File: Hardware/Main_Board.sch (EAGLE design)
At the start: 14 parts

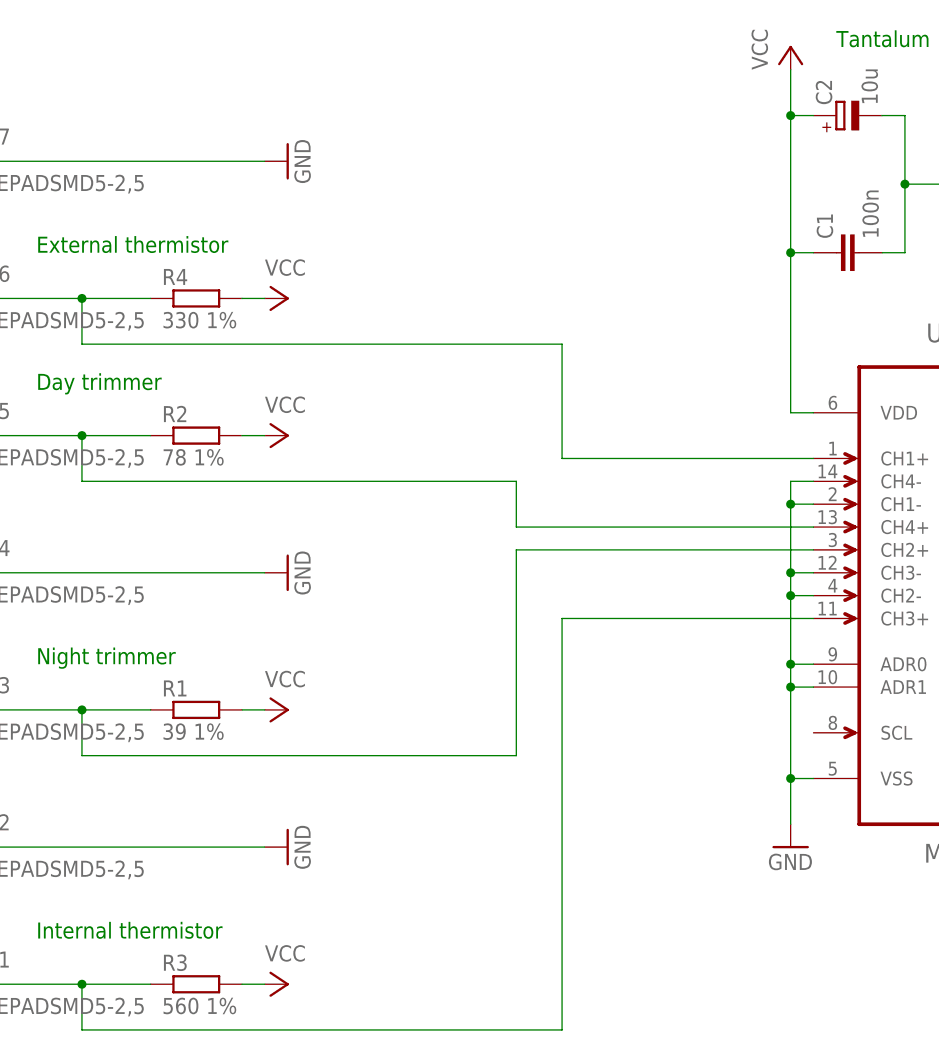
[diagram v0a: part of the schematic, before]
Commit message: Used more generic resistors in the voltage dividers.
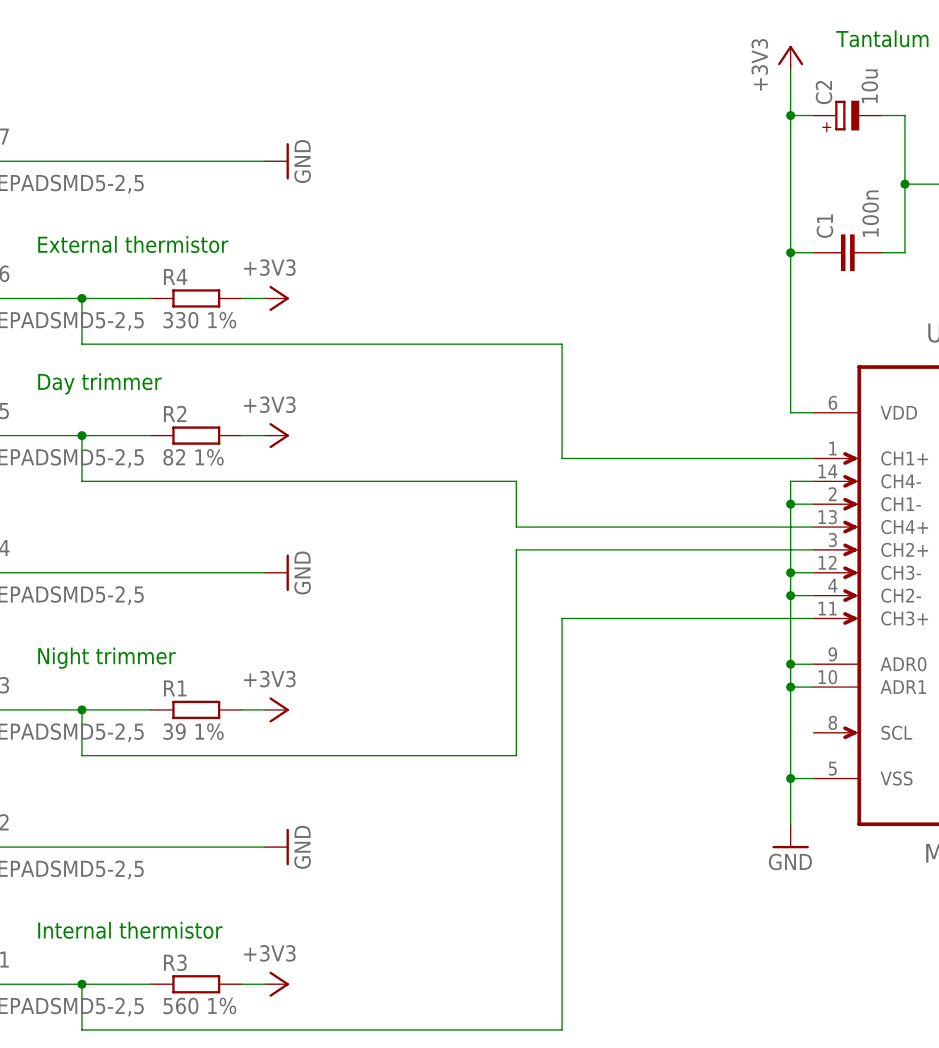
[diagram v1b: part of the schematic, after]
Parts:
- R2: value 78 1% -> 82 1%
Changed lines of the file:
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@@
 <part name="R1" library="resistor" deviceset="R-EU_" device="0207/10" value="39 1%"/>
 <part name="PAD3" library="wirepad" deviceset="WIREPAD" device="SMD5-2,5"/>
-<part name="P+1" library="supply1" deviceset="VCC" device=""/>
+<part name="P+1" library="supply1" deviceset="+3V3" device=""/>
 <part name="U$1" library="MCP3428" deviceset="MCP3428-E/SL" device=""/>
 <part name="PAD5" library="wirepad" deviceset="WIREPAD" device="SMD5-2,5"/>
-<part name="R2" library="resistor" deviceset="R-EU_" device="0207/10" value="78 1%"/>
-<part name="P+2" library="supply1" deviceset="VCC" device=""/>
+<part name="R2" library="resistor" deviceset="R-EU_" device="0207/10" value="82 1%"/>
+<part name="P+2" library="supply1" deviceset="+3V3" device=""/>
 <part name="PAD4" library="wirepad" deviceset="WIREPAD" device="SMD5-2,5"/>
 <part name="GND2" library="supply1" deviceset="GND" device=""/>
@@
 <part name="GND3" library="supply1" deviceset="GND" device=""/>
 <part name="R3" library="resistor" deviceset="R-EU_" device="0207/10" value="560 1%"/>
-<part name="P+3" library="supply1" deviceset="VCC" device=""/>
+<part name="P+3" library="supply1" deviceset="+3V3" device=""/>
 <part name="GND4" library="supply1" deviceset="GND" device=""/>
-<part name="P+4" library="supply1" deviceset="VCC" device=""/>
+<part name="P+4" library="supply1" deviceset="+3V3" device=""/>
 <part name="R4" library="resistor" deviceset="R-EU_" device="0207/10" value="330 1%"/>
-<part name="P+5" library="supply1" deviceset="VCC" device=""/>
+<part name="P+5" library="supply1" deviceset="+3V3" device=""/>
 <part name="PAD6" library="wirepad" deviceset="WIREPAD" device="SMD5-2,5"/>
 <part name="PAD7" library="wirepad" deviceset="WIREPAD" device="SMD5-2,5"/>
@@
 <instance part="R1" gate="G$1" x="-17.78" y="124.46"/>
 <instance part="PAD3" gate="G$1" x="-43.18" y="124.46"/>
-<instance part="P+1" gate="VCC" x="-7.62" y="124.46" rot="R270"/>
+<instance part="P+1" gate="G$1" x="-7.62" y="124.46" rot="R270"/>
 <instance part="U$1" gate="A" x="68.58" y="139.7"/>
 <instance part="PAD5" gate="G$1" x="-43.18" y="154.94"/>
 <instance part="R2" gate="G$1" x="-17.78" y="154.94"/>
-<instance part="P+2" gate="VCC" x="-7.62" y="154.94" rot="R270"/>
+<instance part="P+2" gate="G$1" x="-7.62" y="154.94" rot="R270"/>
 <instance part="PAD4" gate="G$1" x="-43.18" y="139.7"/>
 <instance part="GND2" gate="1" x="-7.62" y="139.7" rot="R90"/>
@@
 <instance part="GND3" gate="1" x="-7.62" y="109.22" rot="R90"/>
 <instance part="R3" gate="G$1" x="-17.78" y="93.98"/>
-<instance part="P+3" gate="VCC" x="-7.62" y="93.98" rot="R270"/>
+<instance part="P+3" gate="G$1" x="-7.62" y="93.98" rot="R270"/>
 <instance part="GND4" gate="1" x="48.26" y="109.22"/>
-<instance part="P+4" gate="VCC" x="48.26" y="198.12"/>
+<instance part="P+4" gate="G$1" x="48.26" y="198.12"/>
 <instance part="R4" gate="G$1" x="-17.78" y="170.18"/>
-<instance part="P+5" gate="VCC" x="-7.62" y="170.18" rot="R270"/>
+<instance part="P+5" gate="G$1" x="-7.62" y="170.18" rot="R270"/>
 <instance part="PAD6" gate="G$1" x="-43.18" y="170.18"/>
 <instance part="PAD7" gate="G$1" x="-43.18" y="185.42"/>
@@
 <net name="VCC" class="0">
 <segment>
-<pinref part="P+1" gate="VCC" pin="VCC"/>
+<pinref part="P+1" gate="G$1" pin="+3V3"/>
 <pinref part="R1" gate="G$1" pin="2"/>
 <wire x1="-10.16" y1="124.46" x2="-12.7" y2="124.46" width="0.1524" layer="91"/>
 </segment>
 <segment>
-<pinref part="P+2" gate="VCC" pin="VCC"/>
+<pinref part="P+2" gate="G$1" pin="+3V3"/>
 <pinref part="R2" gate="G$1" pin="2"/>
 <wire x1="-10.16" y1="154.94" x2="-12.7" y2="154.94" width="0.1524" layer="91"/>
 </segment>
 <segment>
-<pinref part="P+3" gate="VCC" pin="VCC"/>
+<pinref part="P+3" gate="G$1" pin="+3V3"/>
 <pinref part="R3" gate="G$1" pin="2"/>
 <wire x1="-10.16" y1="93.98" x2="-12.7" y2="93.98" width="0.1524" layer="91"/>
 </segment>
 <segment>
-<pinref part="P+4" gate="VCC" pin="VCC"/>
+<pinref part="P+4" gate="G$1" pin="+3V3"/>
 <wire x1="48.26" y1="195.58" x2="48.26" y2="190.5" width="0.1524" layer="91"/>
 <pinref part="U$1" gate="A" pin="VDD"/>
@@
 <segment>
 <pinref part="R4" gate="G$1" pin="2"/>
-<pinref part="P+5" gate="VCC" pin="VCC"/>
+<pinref part="P+5" gate="G$1" pin="+3V3"/>
 <wire x1="-12.7" y1="170.18" x2="-10.16" y2="170.18" width="0.1524" layer="91"/>
 </segment>

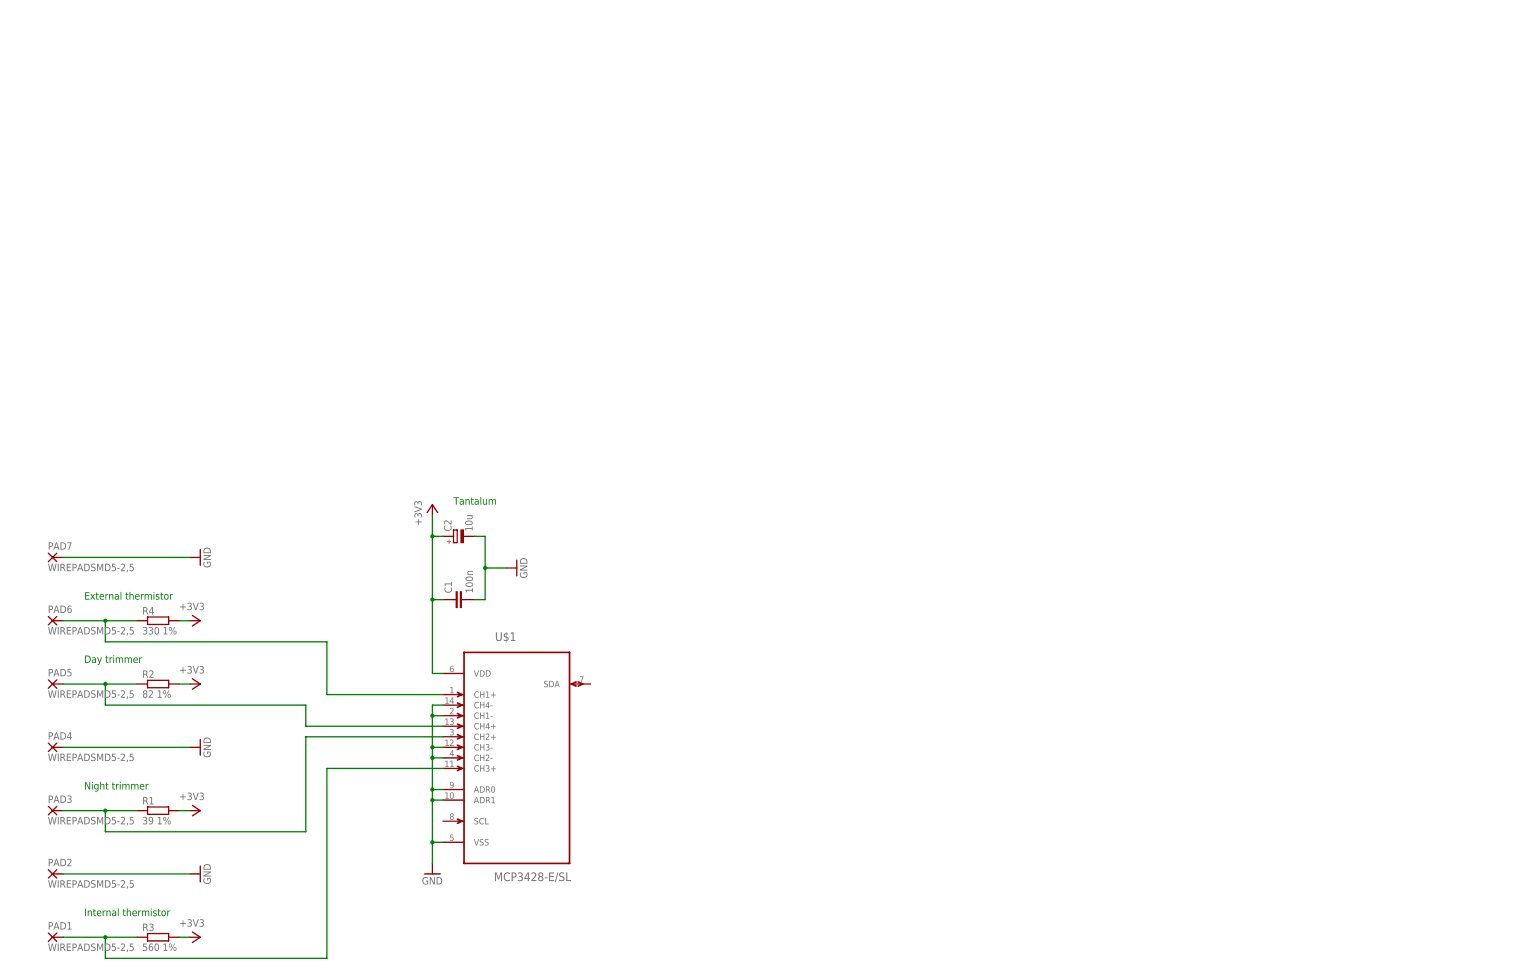
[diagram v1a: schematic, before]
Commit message: Added relay blocks to the schematics.
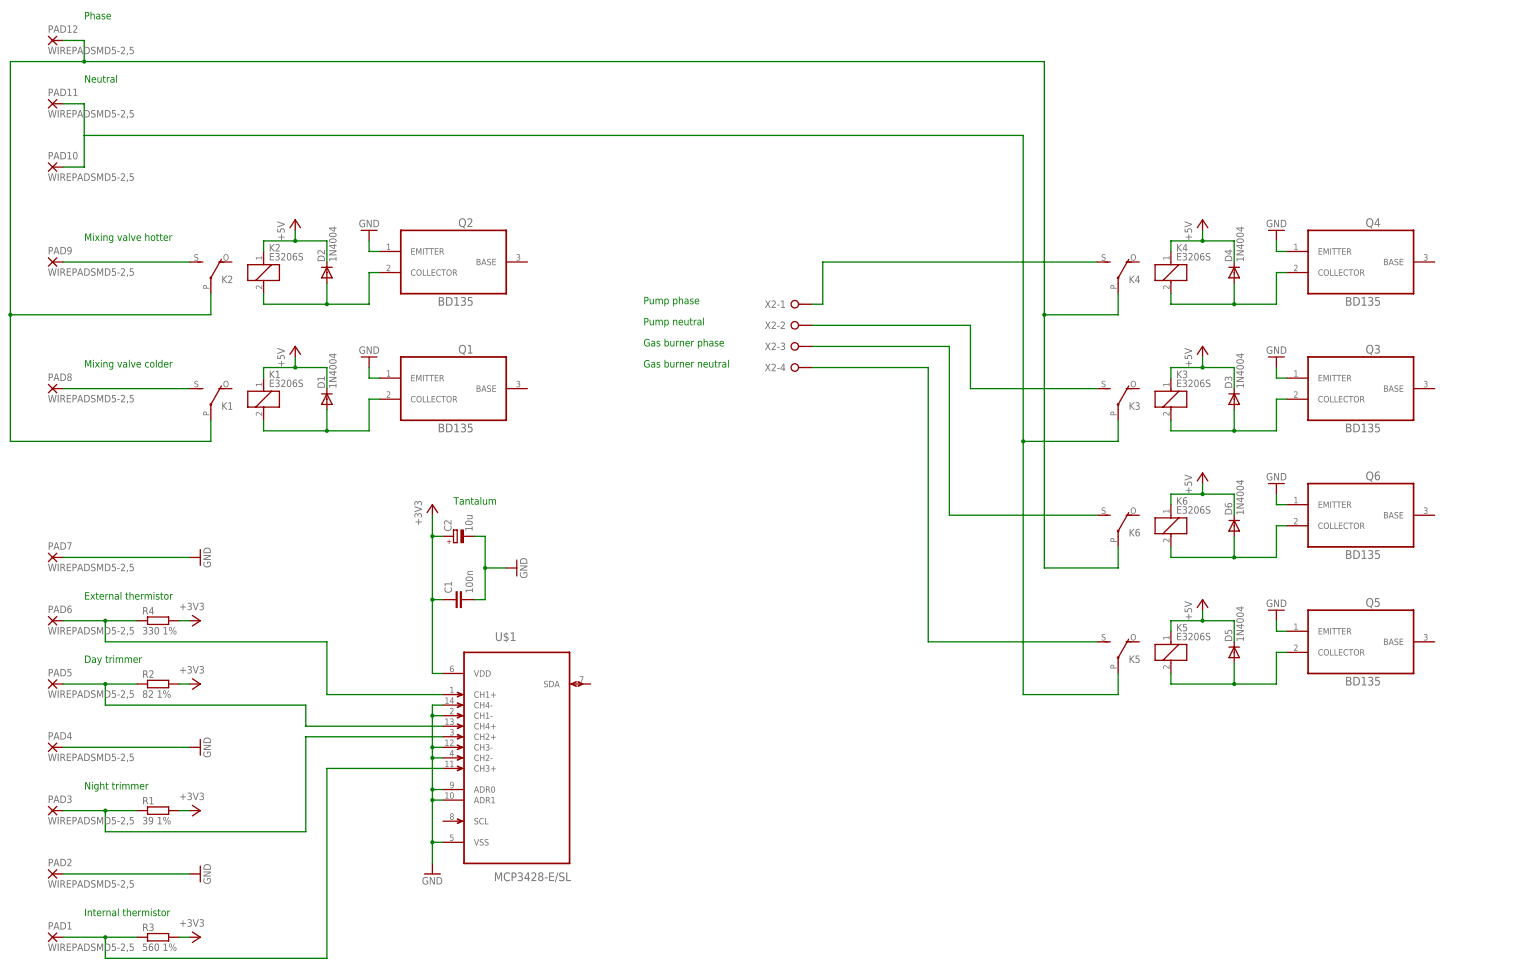
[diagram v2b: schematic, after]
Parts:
- added D1, D2, D3, D4, D5, D6: 1N4004, diode:1N4004
- added K1, K2, K3, K4, K5, K6: E3206S, relay:E3206S
- added PAD10, PAD11, PAD12, PAD8, PAD9: WIREPADSMD5-2,5, wirepad:WIREPADSMD5-2,5
- added Q1, Q2, Q3, Q4, Q5, Q6: BD135, BD135:BD135
- added X2: (no value), con-wago-508:W237-04P
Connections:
- new net +5V: D1.C, D2.C, D3.C, D4.C, D5.C, D6.C, K11.1, K21.1, K31.1, K41.1, K51.1, K61.1
- new net N$10: K12.P, K22.P, K32.P, K42.P, K52.P, K62.P, PAD10.P, PAD11.P, PAD12.P
- new net N$11: K52.S, X2-4.KL
- new net N$12: K32.S, X2-2.KL
- new net N$13: D3.A, K31.2, Q3.COLLECTOR
- new net N$14: K42.S, X2-1.KL
- new net N$15: D4.A, K41.2, Q4.COLLECTOR
- new net N$17: D5.A, K51.2, Q5.COLLECTOR
- new net N$18: K62.S, X2-3.KL
- new net N$19: D6.A, K61.2, Q6.COLLECTOR
- new net N$3: K12.S, PAD8.P
- new net N$4: D1.A, K11.2, Q1.COLLECTOR
- new net N$6: K22.S, PAD9.P
- new net N$7: D2.A, K21.2, Q2.COLLECTOR
- net GND: now also Q1.EMITTER, Q2.EMITTER, Q3.EMITTER, Q4.EMITTER, Q5.EMITTER, Q6.EMITTER
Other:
- note added: "Gas burner neutral"
- note added: "Gas burner phase"
- note added: "Mixing valve colder"
- note added: "Mixing valve hotter"
- note added: "Neutral"
- note added: "Phase"
- note added: "Pump neutral"
- note added: "Pump phase"

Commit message: Used an ATMEGA328 microcontroller to sample analog signals and to control the relays.
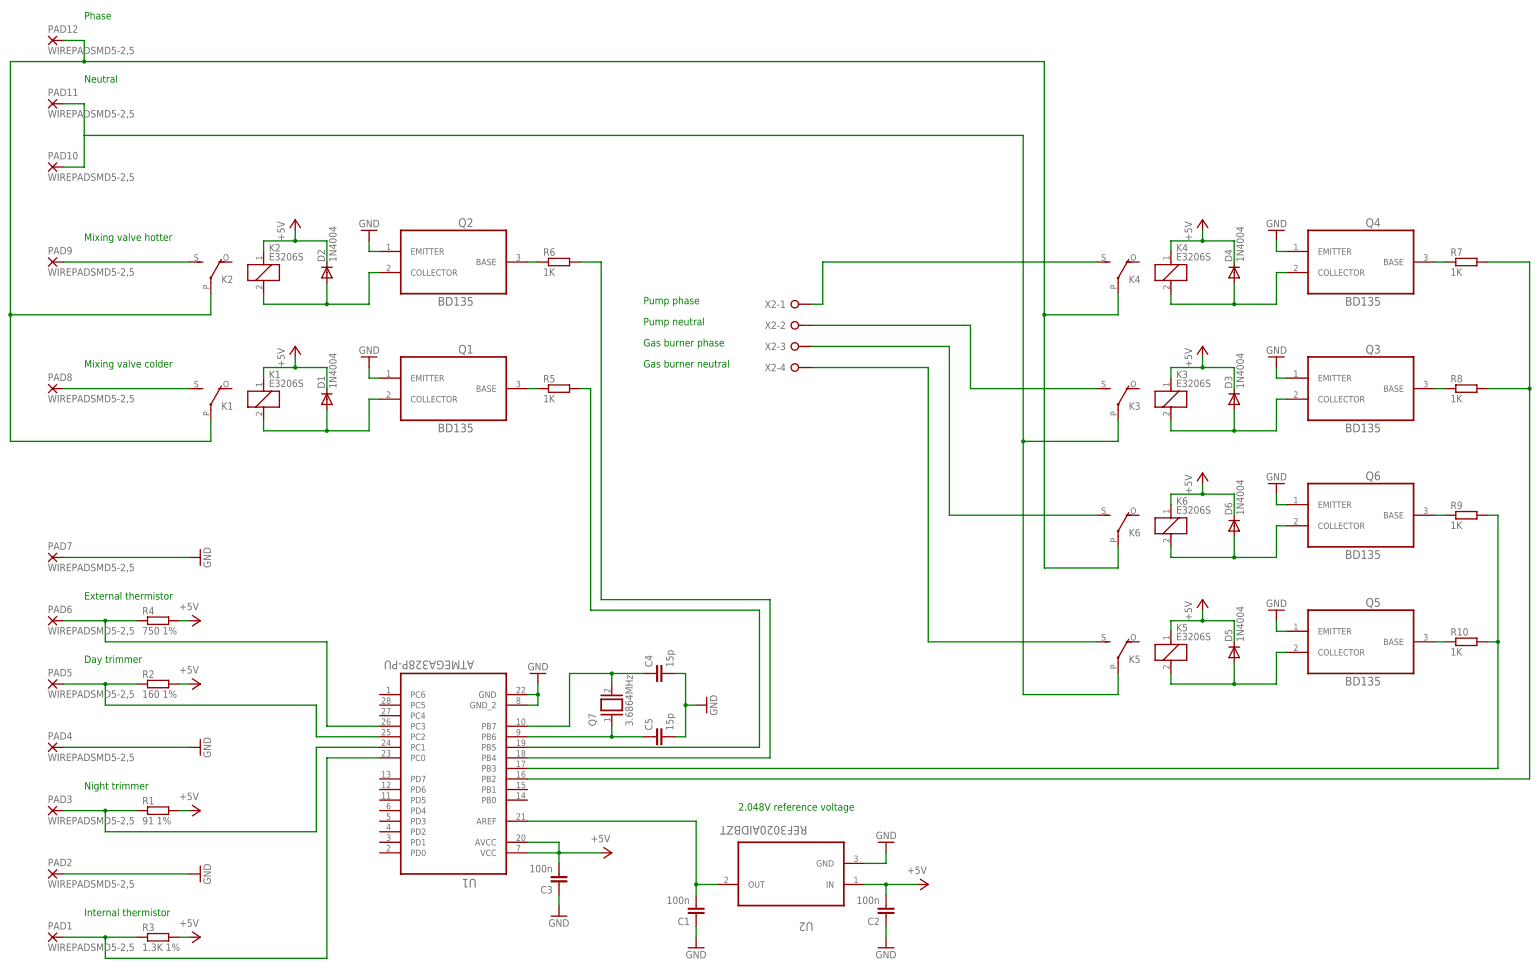
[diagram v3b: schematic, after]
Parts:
- removed U$1: MCP3428-E/SL, MCP3428:MCP3428-E/SL
- added C3: 100n, rcl:C-EU050-035X075
- added C4, C5: 15p, rcl:C-EU025-030X050
- added Q7: 3.6864MHz, special:XTAL/S
- added R10, R5, R6, R7, R8, R9: 1K, resistor:R-EU_0207/10
- added U1: ATMEGA328P-PU, ATMEGA328P-PU:ATMEGA328P-PU
- added U2: REF3020AIDBZT, REF3020AIDBZT:REF3020AIDBZT
- C2: value 10u -> 100n; device rcl:CPOL-EUB45181B -> rcl:C-EU050-035X075
- R1: value 39 1% -> 91 1%
- R2: value 82 1% -> 160 1%
- R3: value 560 1% -> 1.3K 1%
- R4: value 330 1% -> 750 1%
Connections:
- new net N$16: C1.2, U1.AREF, U2.OUT
- new net N$20: Q2.BASE, R6.1
- new net N$21: R5.2, U1.PB5
- new net N$22: R6.2, U1.PB4
- new net N$23: R10.2, R9.2, U1.PB3
- new net N$24: Q5.BASE, R10.1
- new net N$25: Q6.BASE
- new net N$26: R7.2, R8.2, U1.PB2
- new net N$27: C4.1, Q7.2, U1.PB7
- new net N$28: Q3.BASE, R8.1
- new net N$29: C5.1, Q7.1, U1.PB6
- new net N$5: Q4.BASE, R7.1
- new net N$9: Q1.BASE, R5.1
- net +5V: now also C2.2, C3.2, U1.AVCC, U1.VCC, U2.IN
- net GND: now also C1.1, C2.1, C3.1, C4.2, C5.2, U1.GND, U1.GND_2, U2.GND; no longer C1.2, C2.-, U$1.ADR0, U$1.ADR1, U$1.CH1-, U$1.CH2-, U$1.CH3-, U$1.CH4-, U$1.VSS
- net N$1: now also U1.PC2; no longer U$1.CH4+
- net N$2: now also U1.PC0; no longer U$1.CH3+
- net N$8: now also U1.PC3; no longer U$1.CH1+
- net PIN4: now also U1.PC1; no longer U$1.CH2+
- net VCC: no longer C1.1, C2.+, U$1.VDD
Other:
- note added: "2.048V reference voltage"
- note removed: "Tantalum"
- moved on the sheet: C1

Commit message: Replaced +5V supply signal by Vcc for more coherency.
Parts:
- X2: value (none) -> Pump and gas burner
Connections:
- removed net +5V: C2.2, C3.2, D1.C, D2.C, D3.C, D4.C, D5.C, D6.C, K11.1, K21.1, K31.1, K41.1, K51.1, K61.1, U1.AVCC, U1.VCC, U2.IN
- new net N$31: K32.P, K52.P, PAD10.P, PAD11.P
- net N$10: no longer K32.P, K52.P, PAD10.P, PAD11.P
- net N$25: now also R9.1
- net VCC: now also C2.2, C3.2, D1.C, D2.C, D3.C, D4.C, D5.C, D6.C, K11.1, K21.1, K31.1, K41.1, K51.1, K61.1, U1.AVCC, U1.VCC, U2.IN

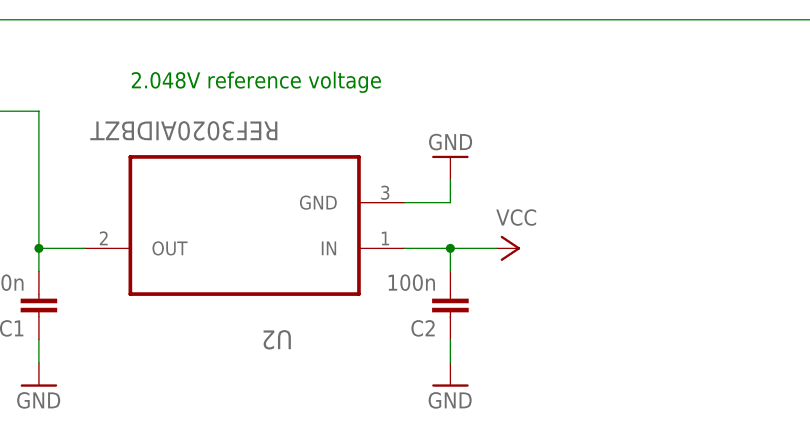
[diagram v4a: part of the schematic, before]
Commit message: Fixed reference voltage input pin capacitor value.
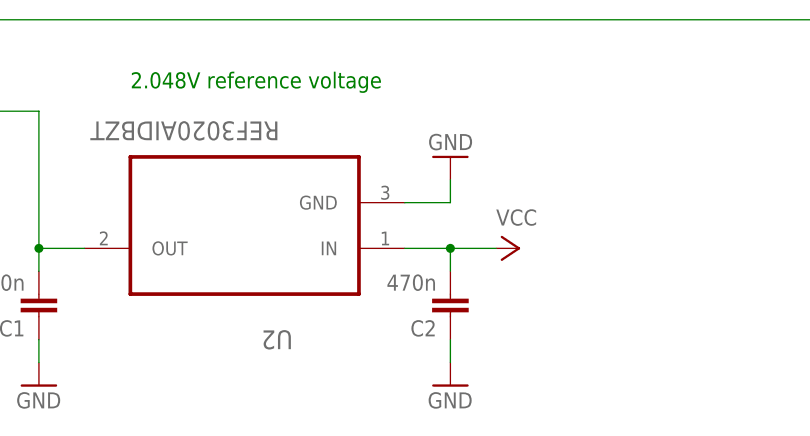
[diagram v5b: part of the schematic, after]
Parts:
- C2: value 100n -> 470n
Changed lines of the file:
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@@
 <part name="C1" library="rcl" deviceset="C-EU" device="050-035X075" value="100n"/>
 <part name="GND1" library="supply1" deviceset="GND" device=""/>
-<part name="C2" library="rcl" deviceset="C-EU" device="050-035X075" value="100n"/>
+<part name="C2" library="rcl" deviceset="C-EU" device="050-035X075" value="470n"/>
 <part name="GND4" library="supply1" deviceset="GND" device=""/>
 <part name="GND14" library="supply1" deviceset="GND" device=""/>
